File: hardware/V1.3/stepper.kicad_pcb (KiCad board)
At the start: 4 copper layers, 40 x 40 mm, 119 parts, among them J101 USB-MINI-B-SMD, J102 DRILL, J103 DRILL, J104 DRILL, J105 DRILL, J401 STACK-UP-HIGH, J402 STACK-DOWN, J403 STACK-UP-HIGH, J404 STACK-DOWN, P201 black, P202 green, P301 CON-SENSOR, P302 CON-SENSOR, Q201 FDS8449, Q202 AO4421, Q203 2N7002, SW101 Reset, SW102 Erase, U101 AT91SAM3SXB, U102 82400152, U201 ZXCT1086, U202 TMC21XX, U501 LD1117, X101 16Mhz

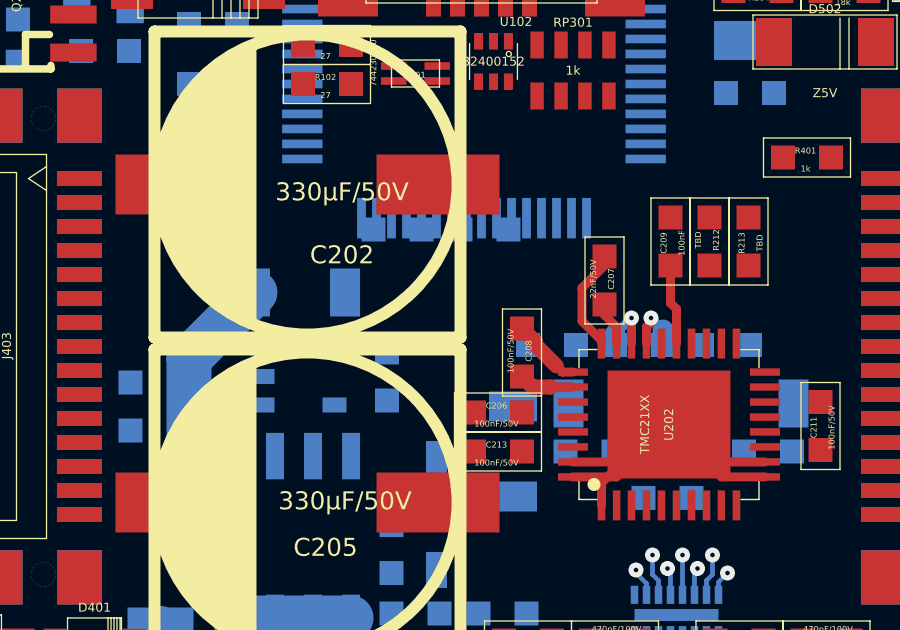
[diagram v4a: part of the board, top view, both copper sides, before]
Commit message: changed placement
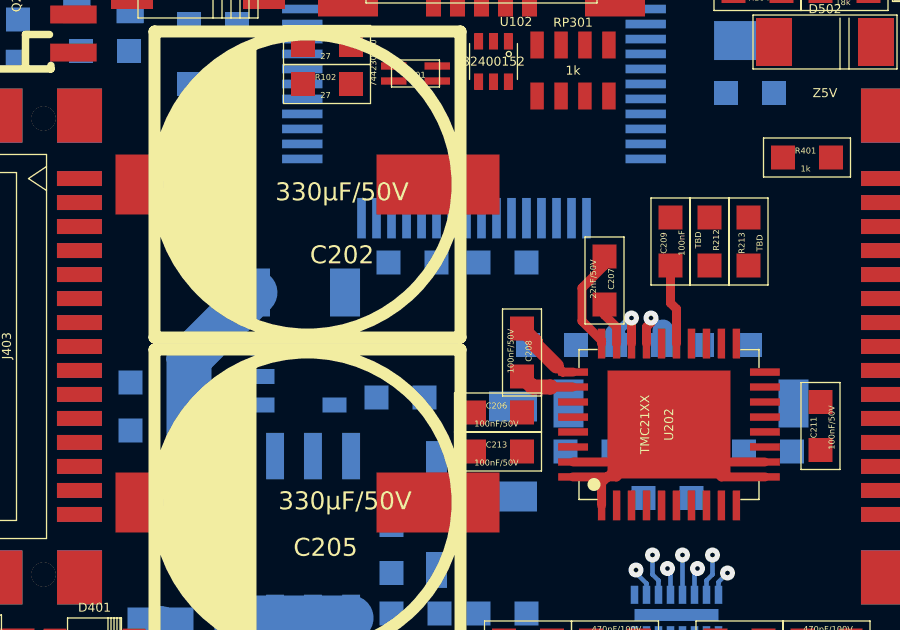
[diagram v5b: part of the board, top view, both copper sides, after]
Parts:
- moved C505 1.25 mm to (147.4, 90.0)
- moved C507 1.21 mm to (144.4, 90.0)
- moved R210 0.83 mm to (144.0, 94.5), turned to 180 degrees

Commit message: partial routing
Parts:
- C206, C208, C213: moved to B.Cu
- moved R210 5.83 mm to (138.2, 93.9), turned to 270 degrees
- moved C215 4.08 mm to (145.1, 93.2), turned to 90 degrees
- moved C206 2.08 mm to (146.9, 93.0), turned to 90 degrees
- moved C203 1.45 mm to (150.3, 92.0), turned to 90 degrees
- moved R205 1.11 mm to (144.5, 100.3), turned to 0 degrees
- moved C213 1.05 mm to (148.2, 95.8), turned to 270 degrees
- moved D201 0.96 mm to (146.0, 97.9), turned to 180 degrees
- moved C218 0.91 mm to (151.2, 96.5)
- moved C217 0.76 mm to (155.5, 96.5)
- moved C207 0.51 mm to (150.9, 90.1), turned to 180 degrees
- moved C201 0.40 mm to (153.3, 97.8)
- moved C204 0.40 mm to (155.2, 92.8)
- moved R211 0.40 mm to (152.3, 92.8)
- moved R215 0.40 mm to (151.5, 94.7)
- moved U202 0.40 mm to (153.3, 95.4)
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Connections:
- net Net-(C202-Pad1) renamed VEE
- net Net-(C210-Pad2) renamed M4
- net Net-(C212-Pad2) renamed M3
- net Net-(C214-Pad2) renamed M2
- net Net-(C216-Pad2) renamed M1
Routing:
- net VEE: track 2.94 -> 36.3 mm, vias 0 -> 9
- net 3V3: track 2.11 -> 16.5 mm, vias 0 -> 2
- net M1: track 0.00 -> 12.1 mm
- net Net-(D203-Pad1): track 3.04 -> 13.0 mm
- net M2: track 0.00 -> 8.43 mm
- net Net-(C218-Pad2): track 0.00 -> 6.99 mm, vias 0 -> 2
- net Net-(D201-Pad2): track 0.00 -> 5.77 mm
- net Net-(C207-Pad2): track 3.48 -> 0.10 mm
- net Net-(C509-Pad1): track 6.01 -> 8.18 mm
- net GND: track 0.92 -> 3.07 mm, vias 1 -> 3
- net PWR-SDI_CFG1: track 0.00 -> 2.08 mm, vias 0 -> 1
- net BRICKLET-IO0_1: track 0.00 -> 2.08 mm, vias 0 -> 1
- net PWR-SCK_CFG2: track 0.00 -> 2.07 mm, vias 0 -> 1
- net BRICKLET-IO0_3: track 0.00 -> 1.91 mm, vias 0 -> 1
- net BRICKLET-IO0_2/PWM0: track 0.00 -> 1.82 mm, vias 0 -> 1
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- added copper zone on F.Cu, net M1
- added copper zone on F.Cu, net M2
- added copper zone on F.Cu, net VEE

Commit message: Merge branch 'master' of github.com:Tinkerforge/stepper-brick
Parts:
- C101, C102, C103, C104, C201, C203, C209, C217, C218, C301, C302, C303, C304, C401, C402, C403, C404, C503, C506, C507, C508, C510, C511, C512, C513, C515, C517, C518, R101, R102, R103, R104, R202, R203, R204, R205, R206, R207, R208, R210, R211, R212, R213, R401, R501: footprint kicad-libraries:0603 -> kicad-libraries:0402
- moved C203 2.14 mm to (151.6, 93.7), turned to 270 degrees
- moved C211 1.98 mm to (158.4, 93.5), turned to 90 degrees
- moved R207 1.98 mm to (145.7, 100.8), turned to 90 degrees
- moved C518 1.40 mm to (143.3, 74.9), turned to 0 degrees
- moved C204 1.39 mm to (153.9, 92.5), turned to 270 degrees
- moved C201 1.37 mm to (154.6, 97.4), turned to 270 degrees
- moved C217 1.35 mm to (156.8, 96.5), turned to 90 degrees
- moved C218 1.35 mm to (149.8, 96.5), turned to 90 degrees
- moved C511 1.04 mm to (148.6, 74.9), turned to 180 degrees
- moved C207 0.96 mm to (150.4, 90.9)
- moved C503 0.66 mm to (145.1, 74.9)
- moved C509 0.64 mm to (147.9, 73.6)
- moved C510 0.53 mm to (146.9, 74.9)
- moved R206 0.50 mm to (144.3, 101.2)
- moved R211 0.44 mm to (152.5, 92.3)
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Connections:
- C201 pad 1: GND -> STACK-PGND
- U202 pad 13: M4 -> M3
- U202 pad 15: M3 -> M4
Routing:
- net VEE: track 36.3 -> 8.07 mm, vias 9 -> 1
- net M4: track 0.00 -> 19.4 mm
- net M3: track 0.00 -> 17.9 mm
- net M2: track 8.43 -> 17.7 mm
- net Net-(D403-Pad2): track 0.00 -> 7.11 mm, vias 0 -> 1
- net M1: track 12.1 -> 18.9 mm
- net Net-(C403-Pad1): track 0.00 -> 5.04 mm
- net Net-(C218-Pad2): track 6.99 -> 2.10 mm
- net 3V3: track 16.5 -> 11.8 mm, vias 2 -> 1
- net STACK-PGND: track 19.4 -> 24.1 mm, vias 0 -> 2
- net Net-(C303-Pad1): track 0.00 -> 3.35 mm
- net Net-(C207-Pad2): track 0.10 -> 3.00 mm
- net Net-(C217-Pad2): track 0.00 -> 2.62 mm, vias 0 -> 2
- net Net-(C207-Pad1): track 0.00 -> 2.62 mm
- net PWR-DCEN_CFG4: track 0.00 -> 2.48 mm, vias 0 -> 1
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- removed copper zone on F.Cu, net M1
- removed copper zone on F.Cu, net M2

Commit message: partially routed
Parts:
- C211: moved to B.Cu
- moved C208 10.0 mm to (157.7, 96.2), turned to 270 degrees
- moved C207 9.28 mm to (155.6, 98.6), turned to 0 degrees
- moved C218 8.58 mm to (156.9, 91.7), turned to 270 degrees
- moved C217 8.50 mm to (149.8, 91.7), turned to 270 degrees
- moved C201 6.49 mm to (152.4, 91.3), turned to 90 degrees
- moved C203 5.19 mm to (155.7, 96.8), turned to 90 degrees
- moved R211 5.18 mm to (154.4, 97.2), turned to 180 degrees
- moved R215 4.66 mm to (155.7, 93.5), turned to 0 degrees
- moved R214 4.57 mm to (151.2, 93.5), turned to 180 degrees
- moved C204 3.82 mm to (152.9, 96.2), turned to 90 degrees
- moved C211 3.38 mm to (155.7, 95.4), turned to 180 degrees
- moved C512 2.66 mm to (153.7, 82.6), turned to 270 degrees
- moved R208 2.02 mm to (135.8, 84.0), turned to 180 degrees
- moved R104 1.69 mm to (157.2, 79.9)
- moved C206 1.43 mm to (148.2, 92.4)
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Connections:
- U202 pad 13: M3 -> M1
- U202 pad 15: M4 -> M2
- U202 pad 32: M1 -> M3
- U202 pad 34: M2 -> M4
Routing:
- net STACK-PGND: track 24.1 -> 61.6 mm, vias 2 -> 49
- net VEE: track 8.07 -> 24.0 mm, vias 1 -> 5
- net Net-(Q202-PadG): track 0.00 -> 8.60 mm, vias 0 -> 1
- net Net-(D202-Pad1): track 0.00 -> 6.24 mm
- net M3: track 17.9 -> 12.9 mm
- net M4: track 19.4 -> 14.4 mm
- net Net-(C509-Pad1): track 6.64 -> 11.5 mm
- net Net-(C209-Pad2): track 4.78 -> 0.00 mm
- net M2: track 17.7 -> 13.8 mm
- net M1: track 18.9 -> 15.2 mm
- net 3V3: track 11.8 -> 14.9 mm, vias 1 -> 2
- net GND: track 5.02 -> 8.06 mm, vias 1 -> 2
- net Net-(L101-Pad4): track 0.00 -> 2.75 mm
- net Net-(C404-Pad1): track 0.00 -> 2.42 mm
- net Net-(C218-Pad2): track 2.10 -> 4.51 mm
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- removed copper zone on F.Cu, net VEE
